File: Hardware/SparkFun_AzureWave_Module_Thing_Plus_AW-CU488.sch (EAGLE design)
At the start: 60 parts, among them J1 THING_PLUS, J2 LiPo, J3 QWIIC_RA, J5 USB-C, Q1 3.1A/30V/105mΩ, Q2 MBT3904DW1T1, U1 AW-CU488, U2 CP210X, U3 XC6222B331MR-G, U4 MCP73831

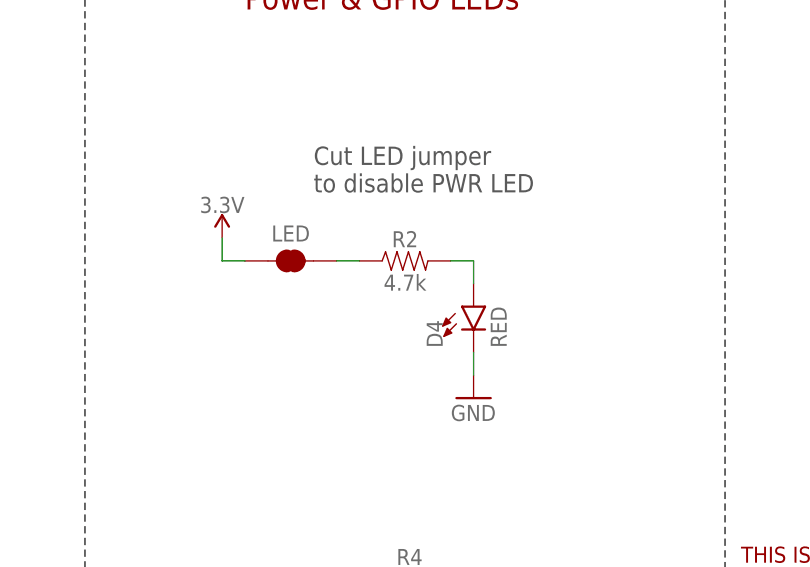
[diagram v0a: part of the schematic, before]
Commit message: RED power LED limiting resistor reduced to 1K for better brightness matching
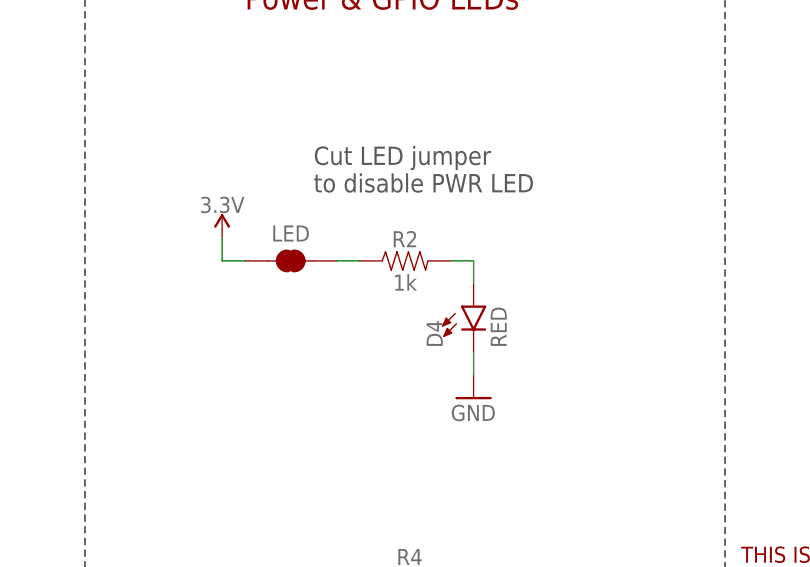
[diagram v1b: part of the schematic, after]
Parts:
- R2: value 4.7k -> 1k; device SparkFun-Resistors:4.7KOHM-0603-1/10W-1% -> SparkFun-Resistors:1KOHM-0402T-1/16W-1%
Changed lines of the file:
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@@
 <part name="USBSHLD" library="SparkFun-Jumpers" deviceset="JUMPER-SMT_2_NC_TRACE" device="_SILK" package3d_urn="urn:adsk.eagle:package:39281/1" value=""/>
 <part name="GND8" library="SparkFun-PowerSymbols" deviceset="GND" device=""/>
-<part name="R2" library="SparkFun-Resistors" deviceset="4.7KOHM" device="-0603-1/10W-1%" value="4.7k"/>
+<part name="R2" library="SparkFun-Resistors" deviceset="1KOHM" device="-0402T-1/16W-1%" value="1k"/>
 <part name="LED" library="SparkFun-Jumpers" deviceset="JUMPER-SMT_2_NC_TRACE" device="_SILK" package3d_urn="urn:adsk.eagle:package:39281/1" value=""/>
 <part name="GND19" library="SparkFun-PowerSymbols" deviceset="GND" device=""/>

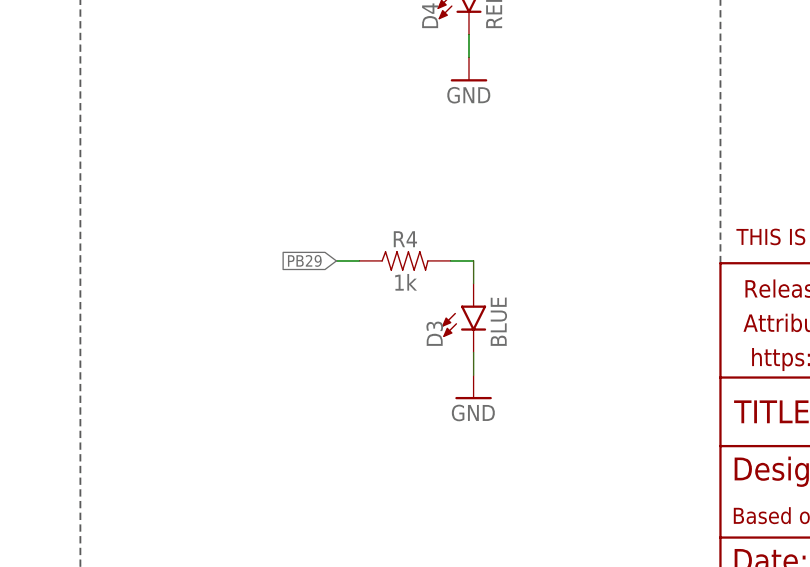
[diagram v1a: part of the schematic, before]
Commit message: Blue LED resistor (R4) corrected to 4.7K
also updated Prod_ID on xc6222 vreg
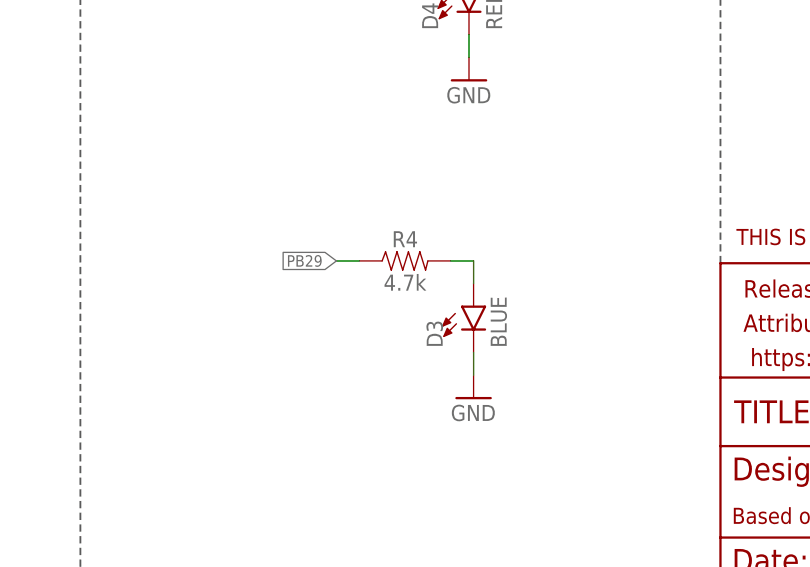
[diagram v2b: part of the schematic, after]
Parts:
- R4: value 1k -> 4.7k; device SparkFun-Resistors:1KOHM-0402T-1/16W-1% -> SparkFun-Resistors:4.7KOHM-0402T-1/16W-1%
- U3: PROD_ID VREG-12457 -> (none)
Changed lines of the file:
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@@
 <part name="D1" library="SparkFun-LED" deviceset="LED-YELLOW" device="0603" value="Yellow"/>
 <part name="R3" library="SparkFun-Resistors" deviceset="4.7KOHM" device="-0402T-1/16W-1%" value="4.7k"/>
-<part name="U3" library="SparkFun-IC-Power" deviceset="XC6222" device="B331MR-G" value="XC6222B331MR-G">
-<attribute name="PROD_ID" value="VREG-12457"/>
-</part>
+<part name="U3" library="SparkFun-IC-Power" deviceset="XC6222" device="B331MR-G" value="XC6222B331MR-G"/>
 <part name="Q1" library="SparkFun-DiscreteSemi" deviceset="MOSFET_PCH" device="-DMG2307L" value="3.1A/30V/105mΩ"/>
 <part name="R6" library="SparkFun-Resistors" deviceset="2.0KOHM" device="-0603-1/10W-5%" value="2.0k"/>
@@
 <part name="C1" library="SparkFun-Capacitors" deviceset="10UF" device="-0402T-6.3V-20%" value="10uF"/>
 <part name="D3" library="SparkFun-LED" deviceset="LED-BLUE" device="0603" value="BLUE"/>
-<part name="R4" library="SparkFun-Resistors" deviceset="1KOHM" device="-0402T-1/16W-1%" value="1k"/>
+<part name="R4" library="SparkFun-Resistors" deviceset="4.7KOHM" device="-0402T-1/16W-1%" value="4.7k"/>
 <part name="GND5" library="SparkFun-PowerSymbols" deviceset="GND" device=""/>
 <part name="R8" library="SparkFun-Resistors" deviceset="100KOHM" device="-0402T-1/16W-1%" value="100k"/>

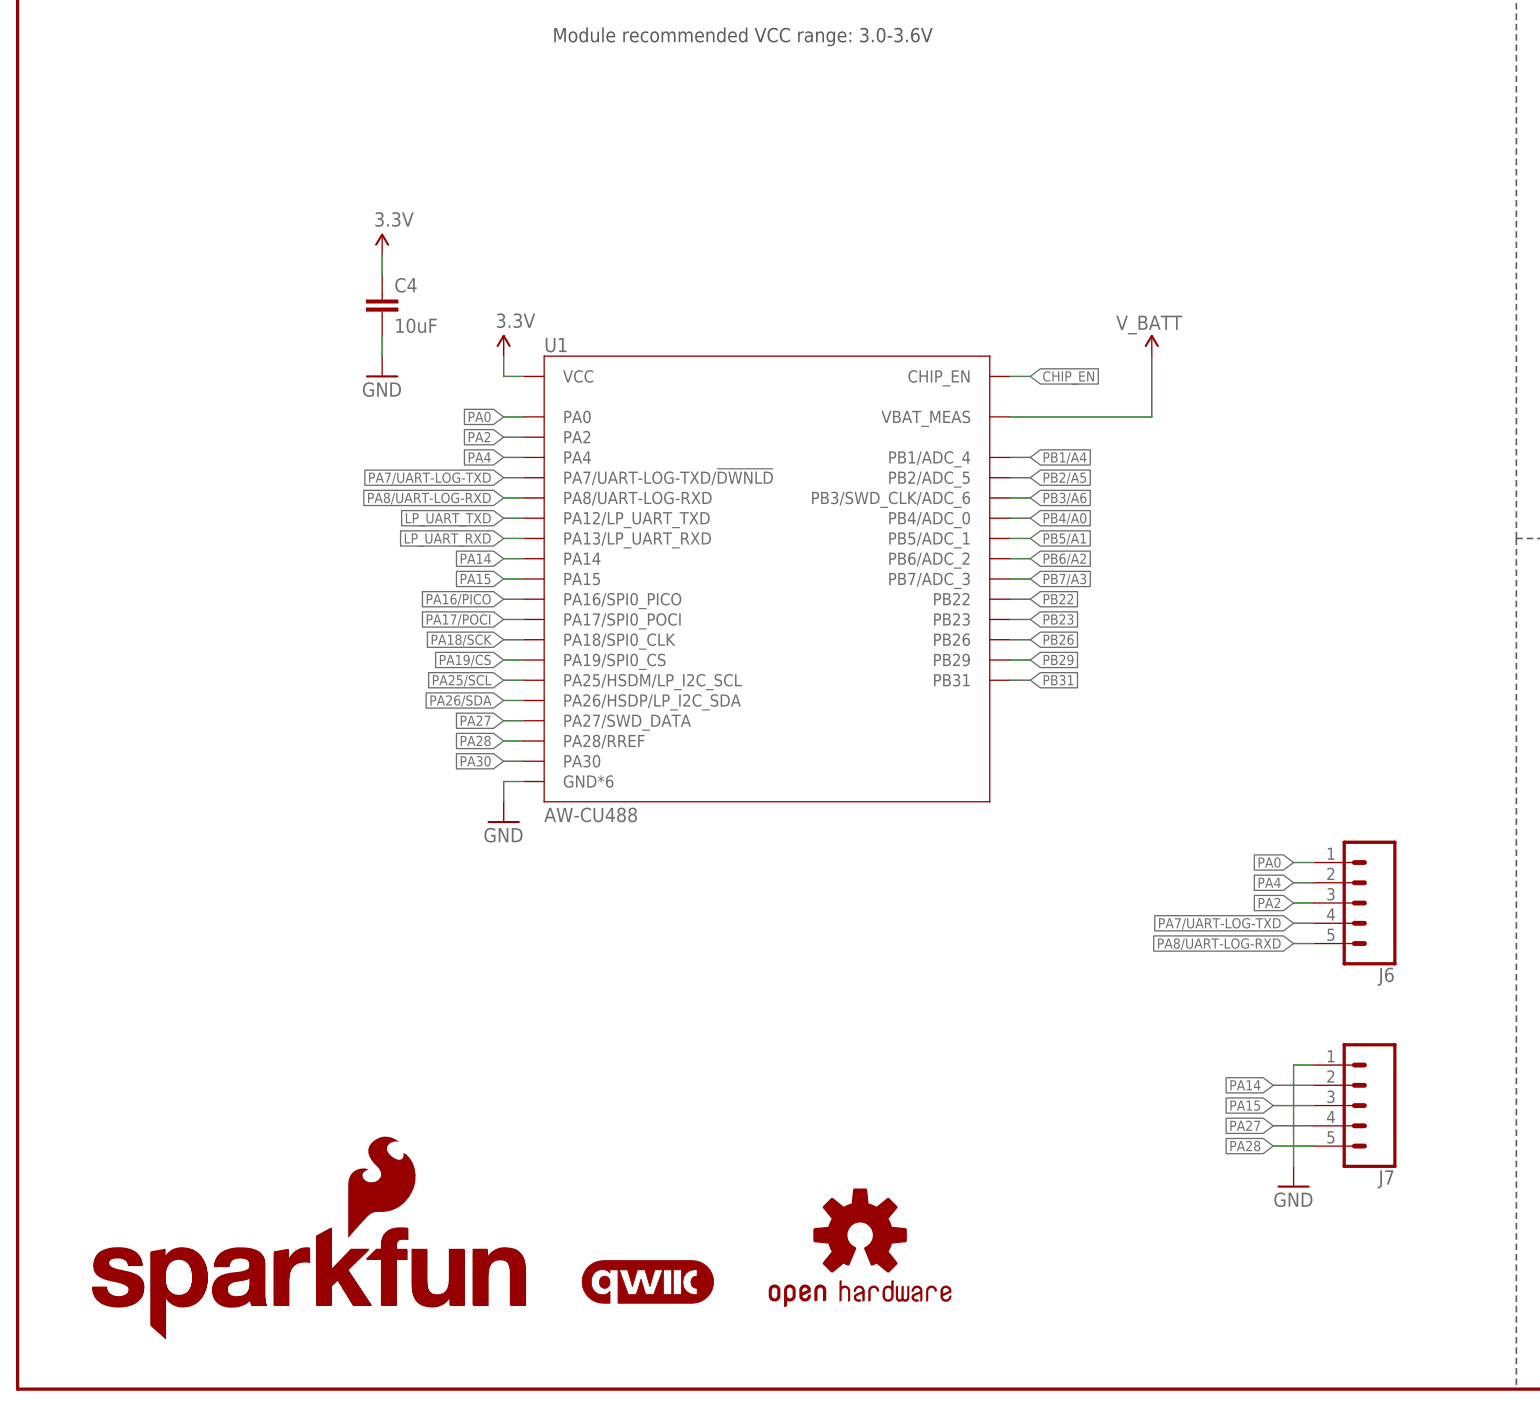
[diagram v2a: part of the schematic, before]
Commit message: added arduino pin mapping table to schematic
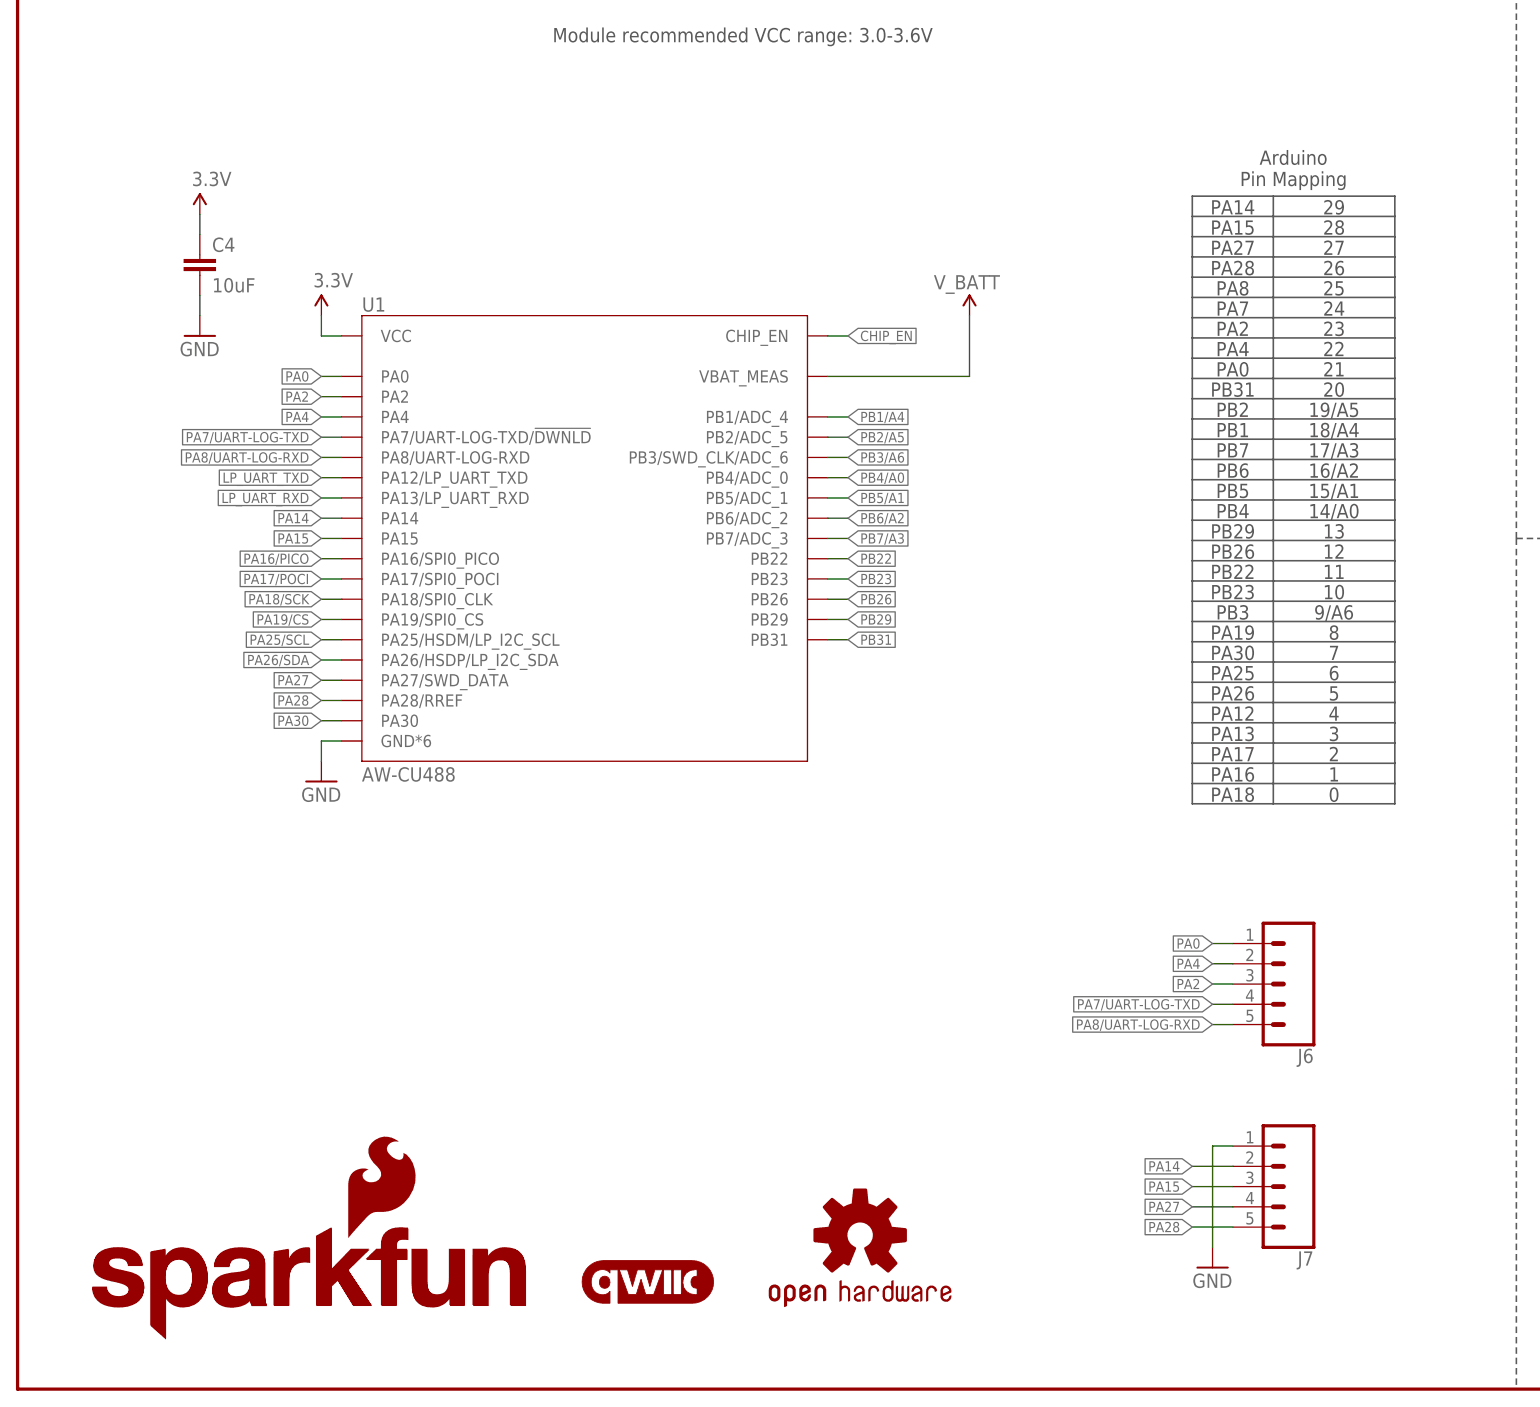
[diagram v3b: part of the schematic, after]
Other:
- note added: "0"
- note added: "1"
- note added: "10"
- note added: "11"
- note added: "12"
- note added: "13"
- note added: "14/A0"
- note added: "15/A1"
- note added: "16/A2"
- note added: "17/A3"
- note added: "18/A4"
- note added: "19/A5"
- note added: "2"
- note added: "20"
- note added: "21"
- note added: "22"
- note added: "23"
- note added: "24"
- note added: "25"
- note added: "26"
- note added: "27"
- note added: "28"
- note added: "29"
- note added: "3"
- note added: "4"
- note added: "5"
- note added: "6"
- note added: "7"
- note added: "8"
- note added: "9/A6"
- note added: "Arduino Pin Mapping"
- note added: "PA0"
- note added: "PA12"
- note added: "PA13"
- note added: "PA14"
- note added: "PA15"
- note added: "PA16"
- note added: "PA17"
- note added: "PA18"
- note added: "PA19"
- note added: "PA2"
- note added: "PA25"
- note added: "PA26"
- note added: "PA27"
- note added: "PA28"
- note added: "PA30"
- note added: "PA4"
- note added: "PA7"
- note added: "PA8"
- note added: "PB1"
- note added: "PB2"
- note added: "PB22"
- note added: "PB23"
- note added: "PB26"
- note added: "PB29"
- note added: "PB3"
- note added: "PB31"
- note added: "PB4"
- note added: "PB5"
- note added: "PB6"
- note added: "PB7"
- moved on the sheet: C4, J6, J7, U1

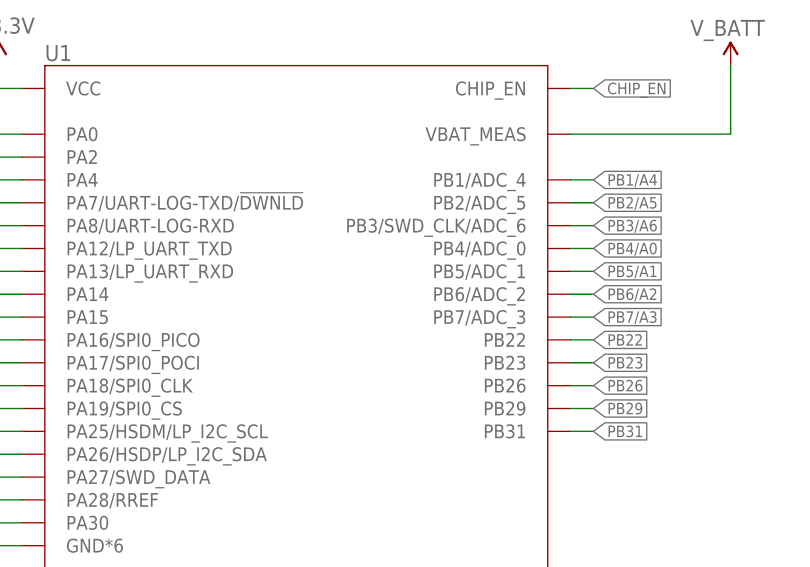
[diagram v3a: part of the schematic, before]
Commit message: Added SPI1 pin-names to device symbol in schematic
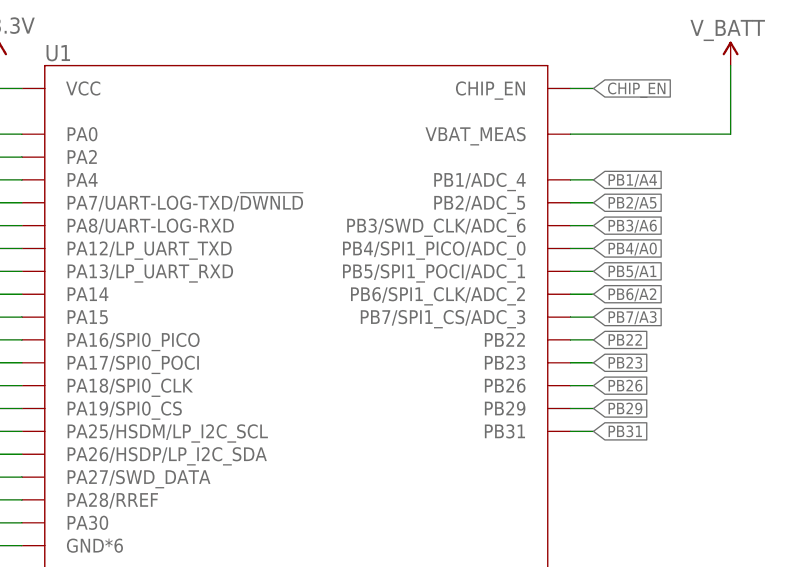
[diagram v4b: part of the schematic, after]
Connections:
- net PB4/A0: now also U1.PB4/SPI1_PICO/ADC_0; no longer U1.PB4/ADC_0
- net PB5/A1: now also U1.PB5/SPI1_POCI/ADC_1; no longer U1.PB5/ADC_1
- net PB6/A2: now also U1.PB6/SPI1_CLK/ADC_2; no longer U1.PB6/ADC_2
- net PB7/A3: now also U1.PB7/SPI1_CS/ADC_3; no longer U1.PB7/ADC_3
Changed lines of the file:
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@@
 <wire x1="101.6" y1="106.68" x2="104.14" y2="106.68" width="0.1524" layer="91"/>
 <label x="104.14" y="106.68" size="1.27" layer="95" font="vector" xref="yes"/>
-<pinref part="U1" gate="U1" pin="PB7/ADC_3"/>
+<pinref part="U1" gate="U1" pin="PB7/SPI1_CS/ADC_3"/>
 </segment>
 <segment>
@@
 <wire x1="101.6" y1="114.3" x2="104.14" y2="114.3" width="0.1524" layer="91"/>
 <label x="104.14" y="114.3" size="1.27" layer="95" font="vector" xref="yes"/>
-<pinref part="U1" gate="U1" pin="PB4/ADC_0"/>
+<pinref part="U1" gate="U1" pin="PB4/SPI1_PICO/ADC_0"/>
 </segment>
 </net>
@@
 <wire x1="101.6" y1="111.76" x2="104.14" y2="111.76" width="0.1524" layer="91"/>
 <label x="104.14" y="111.76" size="1.27" layer="95" font="vector" xref="yes"/>
-<pinref part="U1" gate="U1" pin="PB5/ADC_1"/>
+<pinref part="U1" gate="U1" pin="PB5/SPI1_POCI/ADC_1"/>
 </segment>
 <segment>
@@
 <wire x1="101.6" y1="109.22" x2="104.14" y2="109.22" width="0.1524" layer="91"/>
 <label x="104.14" y="109.22" size="1.27" layer="95" font="vector" xref="yes"/>
-<pinref part="U1" gate="U1" pin="PB6/ADC_2"/>
-</segment>
-<segment>
+<pinref part="U1" gate="U1" pin="PB6/SPI1_CLK/ADC_2"/>
+</segment>
+<segment>
